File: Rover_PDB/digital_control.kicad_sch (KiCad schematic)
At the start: 0 parts

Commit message: add curr teensy schematic, clean files, .gitignore update
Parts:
- added C1: 0.2uF, Capacitor_SMD:C_01005_0402Metric, symbol Device:C_Small
- added C2, C4: 100nF, Capacitor_SMD:C_01005_0402Metric, symbol Device:C_Small
- added C3: 50nF, Capacitor_SMD:C_01005_0402Metric, symbol Device:C_Small
- added J1, J2, J3: Conn_01x04, Connector_Wago:Wago_734-134_1x04_P3.50mm_Vertical, symbol Connector_Generic:Conn_01x04
- added M1, M2, M3: Fan, Connector_JST:JST_XH_B2B-XH-A_1x02_P2.50mm_Vertical, symbol Motor:Fan
- added Q1, Q2: NMOS, Package_TO_SOT_THT:TO-220-3_Vertical, symbol Simulation_SPICE:NMOS
- added R1: 1k, Resistor_SMD:R_01005_0402Metric, symbol Device:R_US
- added R2: 10k, Resistor_SMD:R_01005_0402Metric, symbol Device:R_US
- added R3: 5k1, Resistor_SMD:R_01005_0402Metric, symbol Device:R_US
- added U1: Teensy4.1, teensy:Teensy41, symbol teensy:Teensy4.1
- added U2: MCP9808_MSOP, Package_SO:MSOP-8_3x3mm_P0.65mm, symbol Sensor_Temperature:MCP9808_MSOP
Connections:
- new net: C4.1, C4.2, U1.48 (VIN)
- new net: J2.3 (Pin_3), U1.20 (28_RX7)
- new net: J2.4 (Pin_4), U1.21 (29_TX7)
- new net: R3.1, U2.5 (A2), U2.6 (A1), U2.7 (A0)
- new net: C3.1, Q1.1 (D), Q2.2 (G), R2.2
- new net: Q1.2 (G), R1.2
- new net: J1.3 (Pin_3), U1.2 (0_RX1_CRX2_CS1)
- new net: J1.4 (Pin_4), U1.3 (1_TX1_CTX2_MISO1)
- new net: J3.4 (Pin_4), U1.10 (8_TX2_IN1)
- new net: C2.1, R1.1, U1.44 (22_A8_CTX1)
- new net: J3.3 (Pin_3), U1.9 (7_RX2_OUT1A)
- new net: M1.1 (+), M2.1 (+), M3.1 (+)
- new net: M1.2 (-), M2.2 (-), M3.2 (-), Q2.1 (D)
- new net +3V3: J3.1 (Pin_1), U1.51 (3V3)
- new net GND: C1.1, C1.2, C2.2, C3.2, J3.2 (Pin_2), Q1.3 (S), Q2.3 (S), R3.2, U1.45 (23_A9_CRX1_MCLK1), U1.47 (GND), U1.58 (GND), U1.59 (GND), U2.4 (GND), U2.8 (V_{DD})
- new net SCL: U2.2 (SCL)
- new net SDA: U2.1 (SDA)
- no-connect marks 0 -> 57
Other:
- note added: "1: Vdd 2: Gnd 3: Tx 4: Rx"

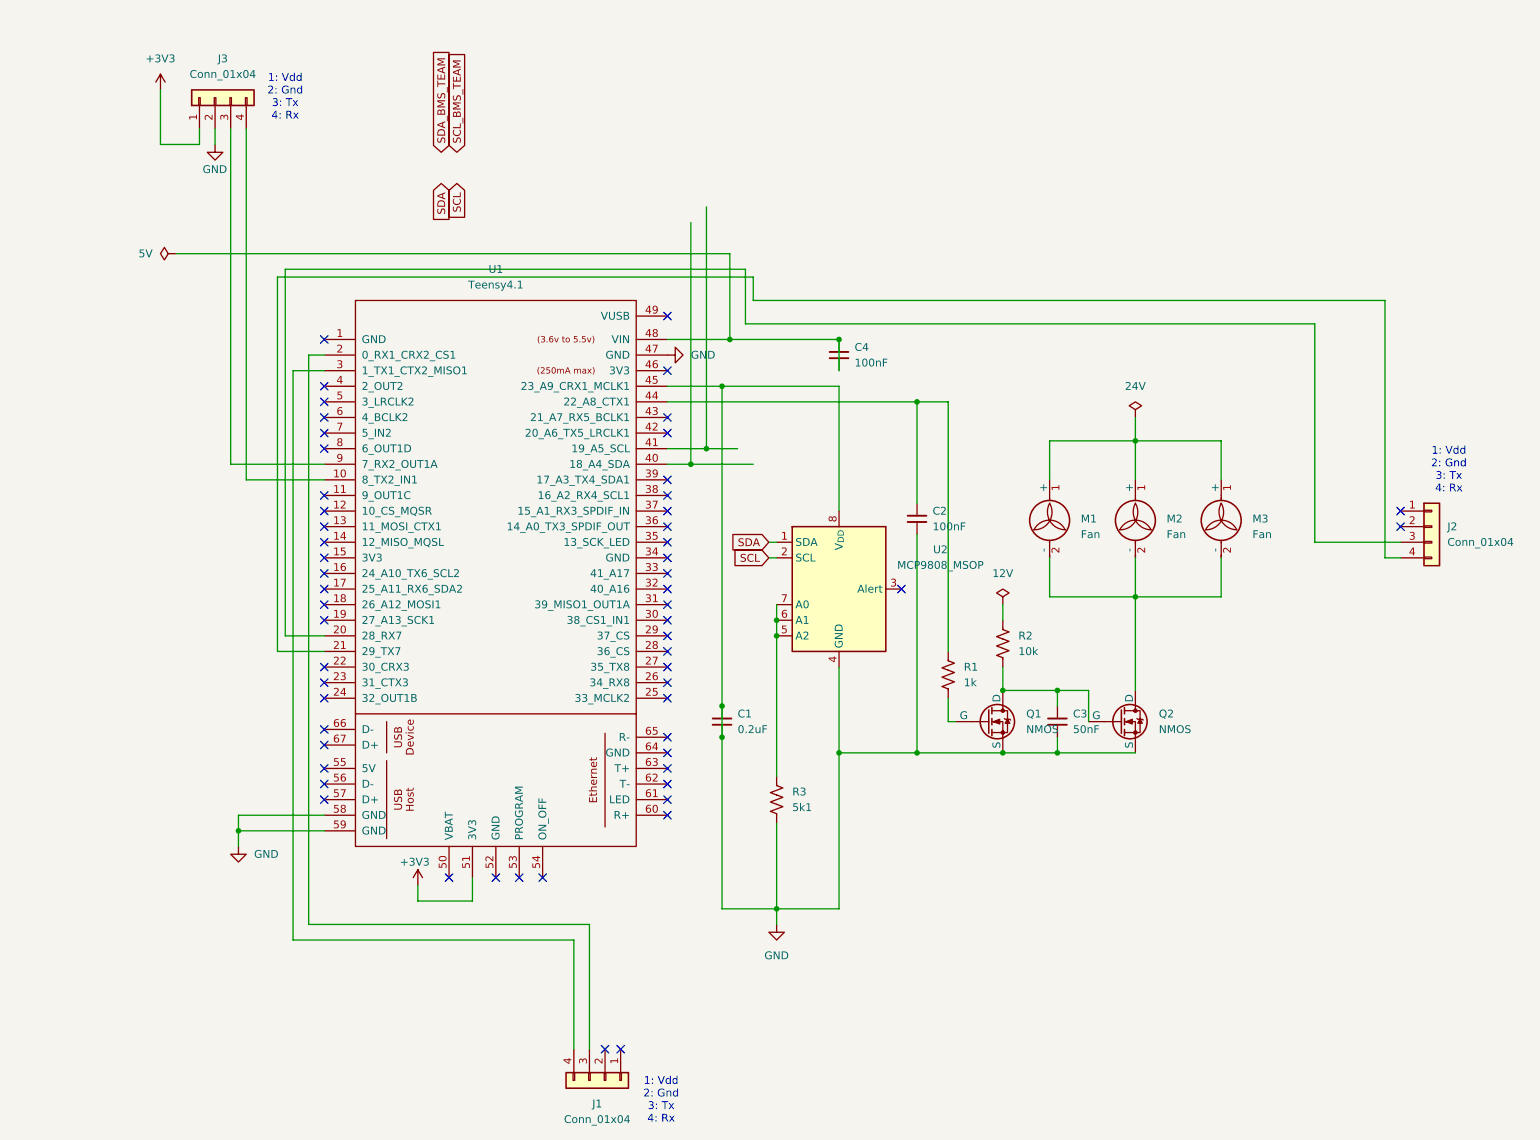
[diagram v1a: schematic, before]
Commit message: move stuff around
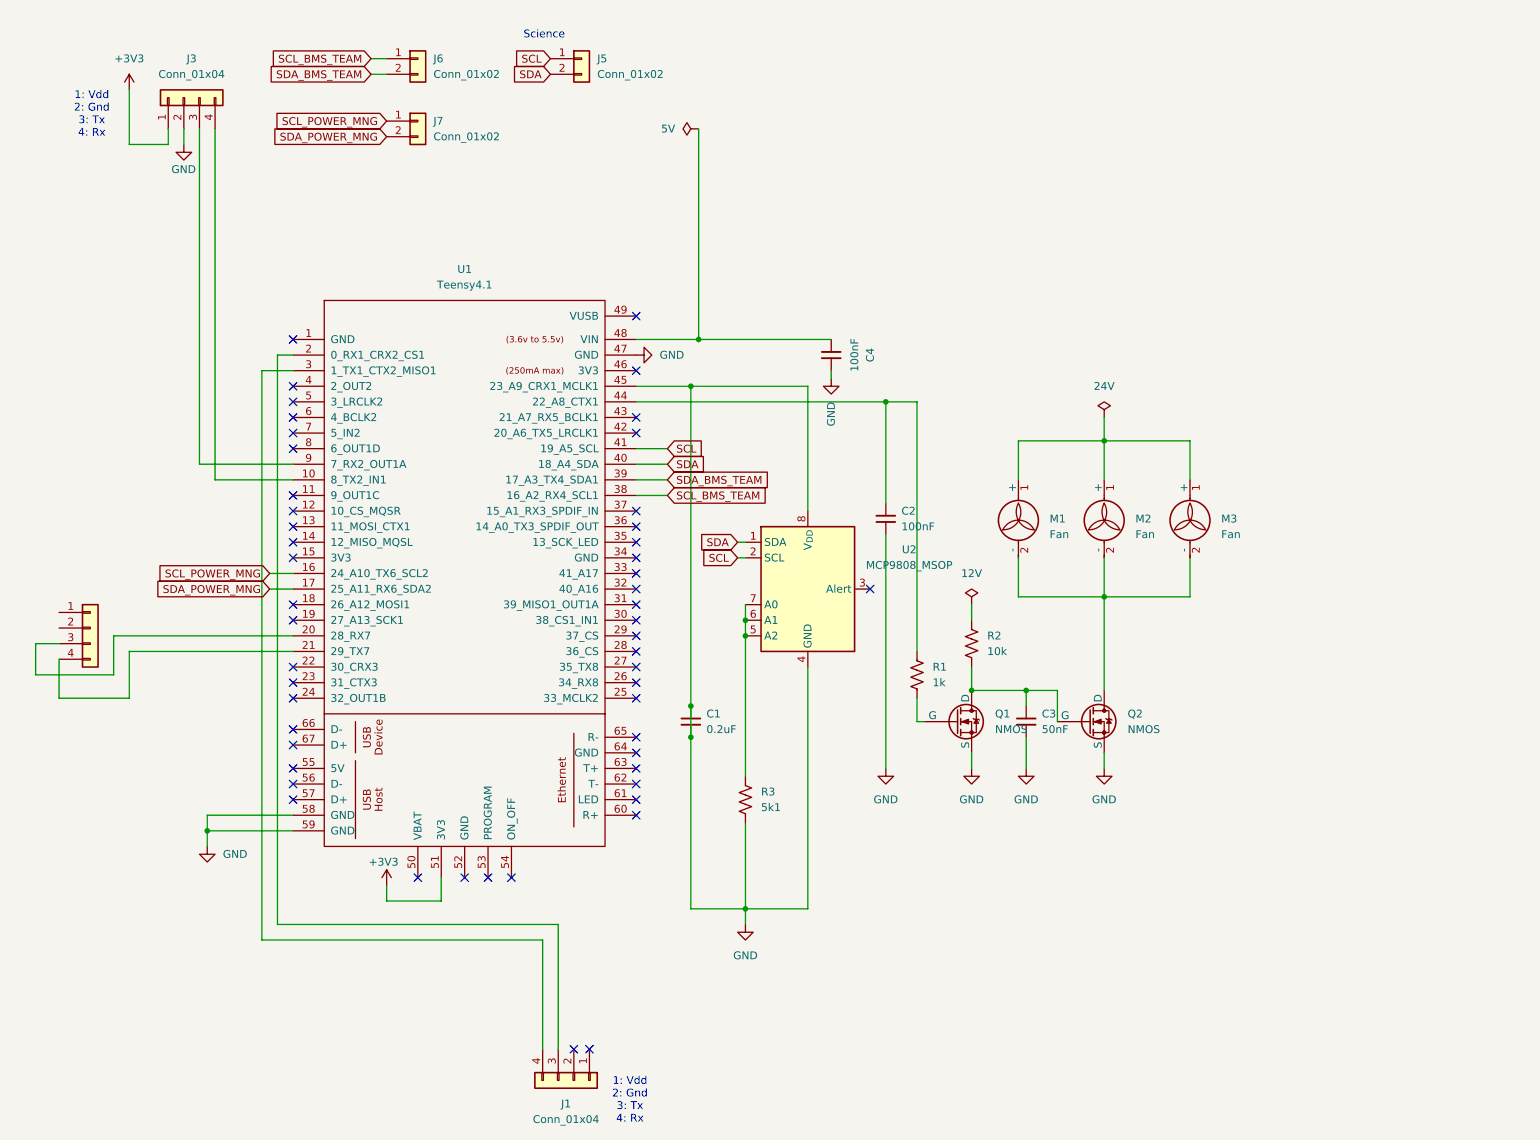
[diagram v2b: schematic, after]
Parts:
- added J5, J6, J7: Conn_01x02, symbol Connector_Generic:Conn_01x02
- M1, M2, M3: footprint Connector_JST:JST_XH_B2B-XH-A_1x02_P2.50mm_Vertical -> TerminalBlock_RND:TerminalBlock_RND_205-00056_1x02_P5.00mm_45Degree
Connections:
- net GND: now also C4.1
- net SCL: now also U1.41 (19_A5_SCL), J5.1 (Pin_1)
- net SCL_BMS_TEAM: now also U1.38 (16_A2_RX4_SCL1), J6.1 (Pin_1)
- net SDA: now also U1.40 (18_A4_SDA), J5.2 (Pin_2)
- net SDA_BMS_TEAM: now also U1.39 (17_A3_TX4_SDA1), J6.2 (Pin_2)
- net at C4.2, U1.48 (VIN): no longer C4.1
- net SCL_POWER_MNG: now reaches U1.16 (24_A10_TX6_SCL2)
- net SCL_POWER_MNG: now also J7.1 (Pin_1)
- net SDA_POWER_MNG: now reaches U1.17 (25_A11_RX6_SDA2)
- net SDA_POWER_MNG: now also J7.2 (Pin_2)
- no-connect marks 57 -> 51
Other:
- note added: "Science"

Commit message: clean schematic
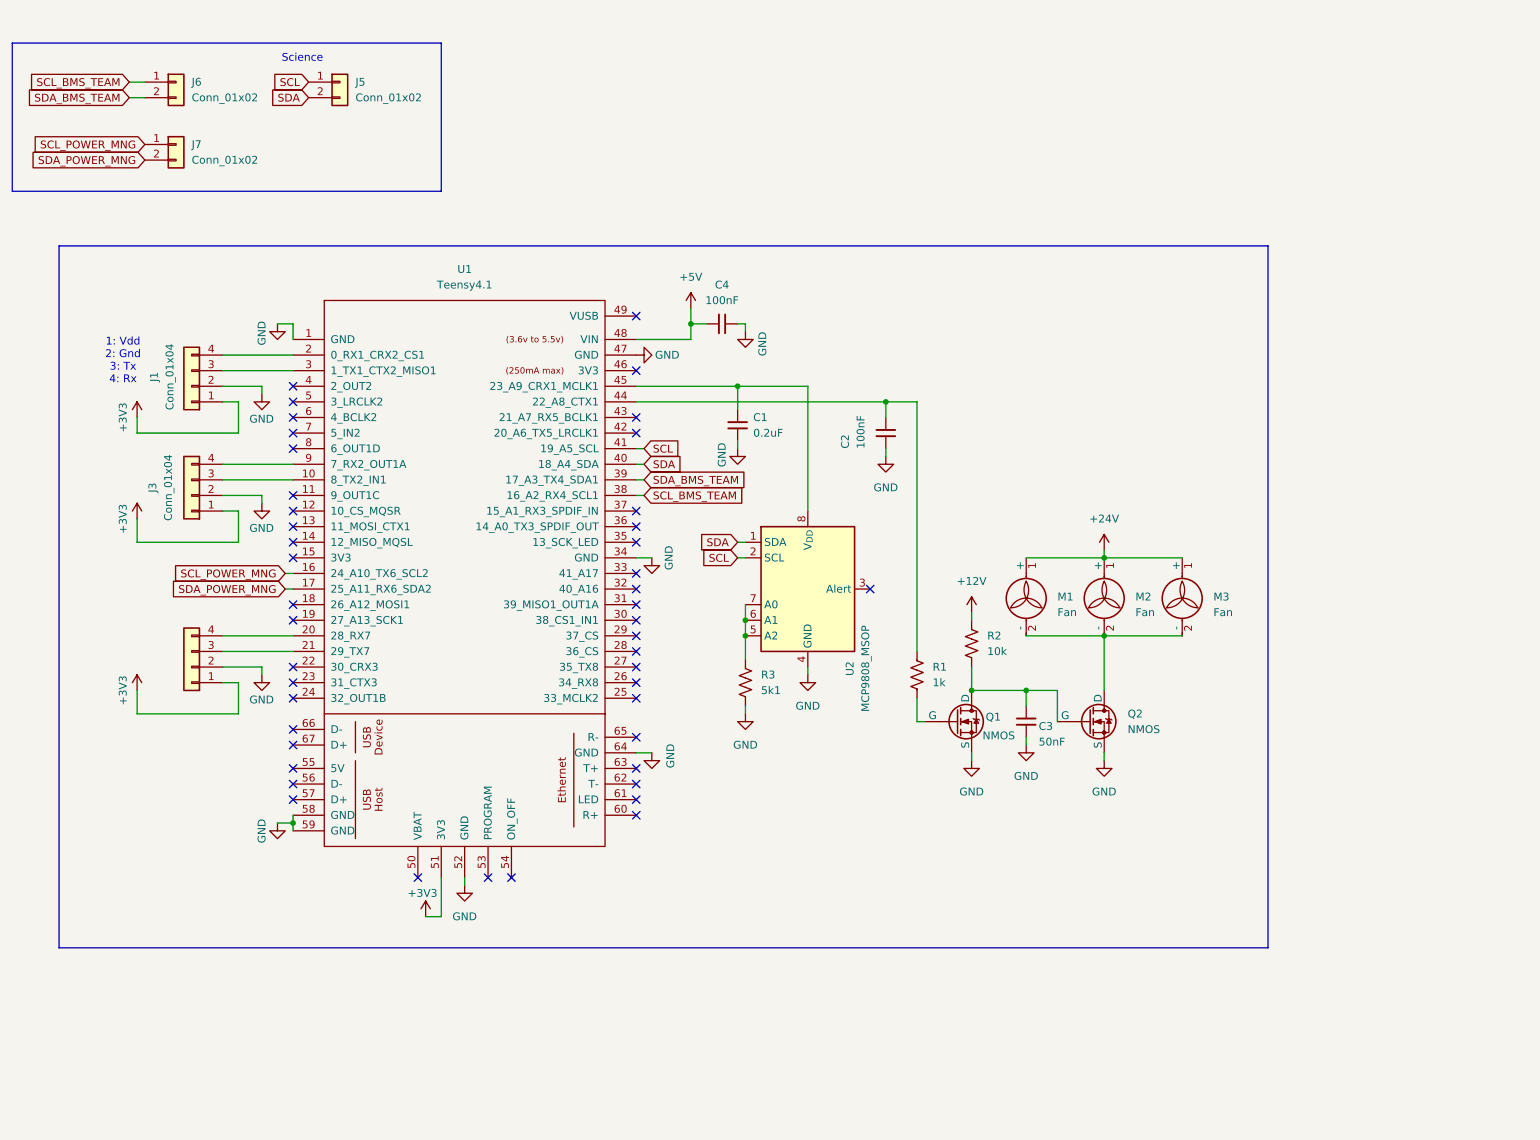
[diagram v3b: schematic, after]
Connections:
- net +3V3: now also J1.1 (Pin_1), J2.1 (Pin_1)
- net GND: now also J1.2 (Pin_2), J2.2 (Pin_2), U1.1 (GND), U1.34 (GND), U1.52 (GND), U1.64 (GND); no longer C1.1, U1.45 (23_A9_CRX1_MCLK1), U2.8 (V_{DD})
- net +5V: now reaches C4.2, U1.48 (VIN)
- net +12V: now reaches R2.1
- net +24V: now reaches M1.1 (+), M2.1 (+), M3.1 (+)
- net at J2.3 (Pin_3): now also U1.21 (29_TX7); no longer U1.20 (28_RX7)
- net at J2.4 (Pin_4): now also U1.20 (28_RX7); no longer U1.21 (29_TX7)
- net at J3.3 (Pin_3): now also U1.10 (8_TX2_IN1); no longer U1.9 (7_RX2_OUT1A)
- net at J3.4 (Pin_4): now also U1.9 (7_RX2_OUT1A); no longer U1.10 (8_TX2_IN1)
- net at J1.3 (Pin_3): now also U1.3 (1_TX1_CTX2_MISO1); no longer U1.2 (0_RX1_CRX2_CS1)
- net at J1.4 (Pin_4): now also U1.2 (0_RX1_CRX2_CS1); no longer U1.3 (1_TX1_CTX2_MISO1)
- new net: C1.1, U1.45 (23_A9_CRX1_MCLK1), U2.8 (V_{DD})
- no-connect marks 51 -> 45
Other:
- moved on the sheet: C1, C2, C4, J1, J3, J5, J6, J7, M1, M2, M3, R3

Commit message: mes
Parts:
- removed J5: Conn_01x02, symbol Connector_Generic:Conn_01x02
- added J4: Conn_01x04, symbol Connector_Generic:Conn_01x04
- added R10, R4, R5, R7, R8, R9: 2k2, symbol Device:R_US
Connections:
- net +3V3: now also R10.1, R4.1, R5.1, R7.1, R8.1, R9.1
- net CS0: now reaches U1.12 (10_CS_MQSR)
- net CS0: now also J4.1 (Pin_1)
- net MOSI0: now reaches U1.13 (11_MOSI_CTX1)
- net MOSI0: now also J4.3 (Pin_3)
- net MISO0: now reaches U1.14 (12_MISO_MQSL)
- net MISO0: now also J4.4 (Pin_4)
- net SCK0: now reaches U1.35 (13_SCK_LED)
- net SCK0: now also J4.2 (Pin_2)
- net SCL renamed SCL_0
- net SCL_0: now also R5.2
- net SCL_BMS_TEAM renamed SCL_1
- net SCL_1: now also R7.2
- net SCL_POWER_MNG renamed SCL_2
- net SCL_2: now also R9.2
- net SDA renamed SDA_0
- net SDA_0: now also R4.2
- net SDA_BMS_TEAM renamed SDA_1
- net SDA_1: now also R8.2
- net SDA_POWER_MNG renamed SDA_2
- net SDA_2: now also R10.2
- no-connect marks 45 -> 41
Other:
- note added: "SPI CS SCLK MOSI MISO"
- note removed: "Science"
- moved on the sheet: J3

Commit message: gpt stuff
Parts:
- removed C3: 50nF, Capacitor_SMD:C_01005_0402Metric, symbol Device:C_Small
- added D1: SS14, symbol Device:D
- added R6: R_Small_US, Package_DIP:DIP-8_W7.62mm, symbol Device:R_Small_US
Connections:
- net +24V: now also D1.1 (K)
- net +3V3: now also C1.1, U2.8 (V_{DD})
- net at R1.1, U1.44 (22_A8_CTX1): now also R6.2; no longer C2.1
- net at M1.2 (-), M2.2 (-), M3.2 (-)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: now also D1.2 (A)
- new net: C2.1, R6.1
- now unconnected: U1.45 (23_A9_CRX1_MCLK1)
- no-connect marks 41 -> 42
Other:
- moved on the sheet: C1, C2
